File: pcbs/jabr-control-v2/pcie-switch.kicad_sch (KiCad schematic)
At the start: 41 parts, among them U301 SYA75603A, U302 PCI11010C, Y301 XRCGB25M000F3A16R0

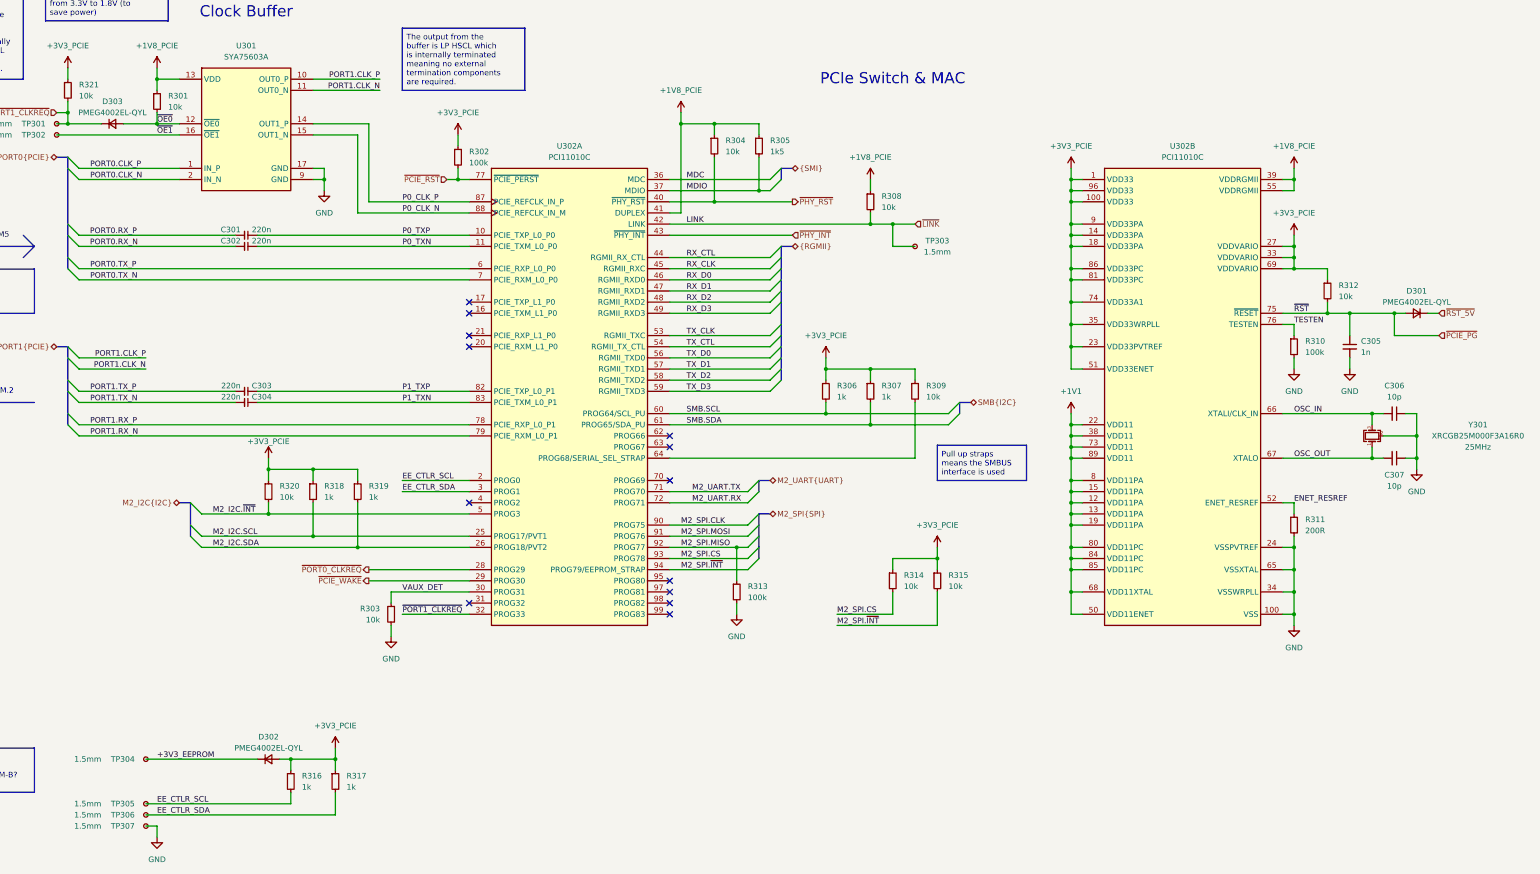
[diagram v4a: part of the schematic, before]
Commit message: Removed power button reset to switch (power will be cycled anyway)
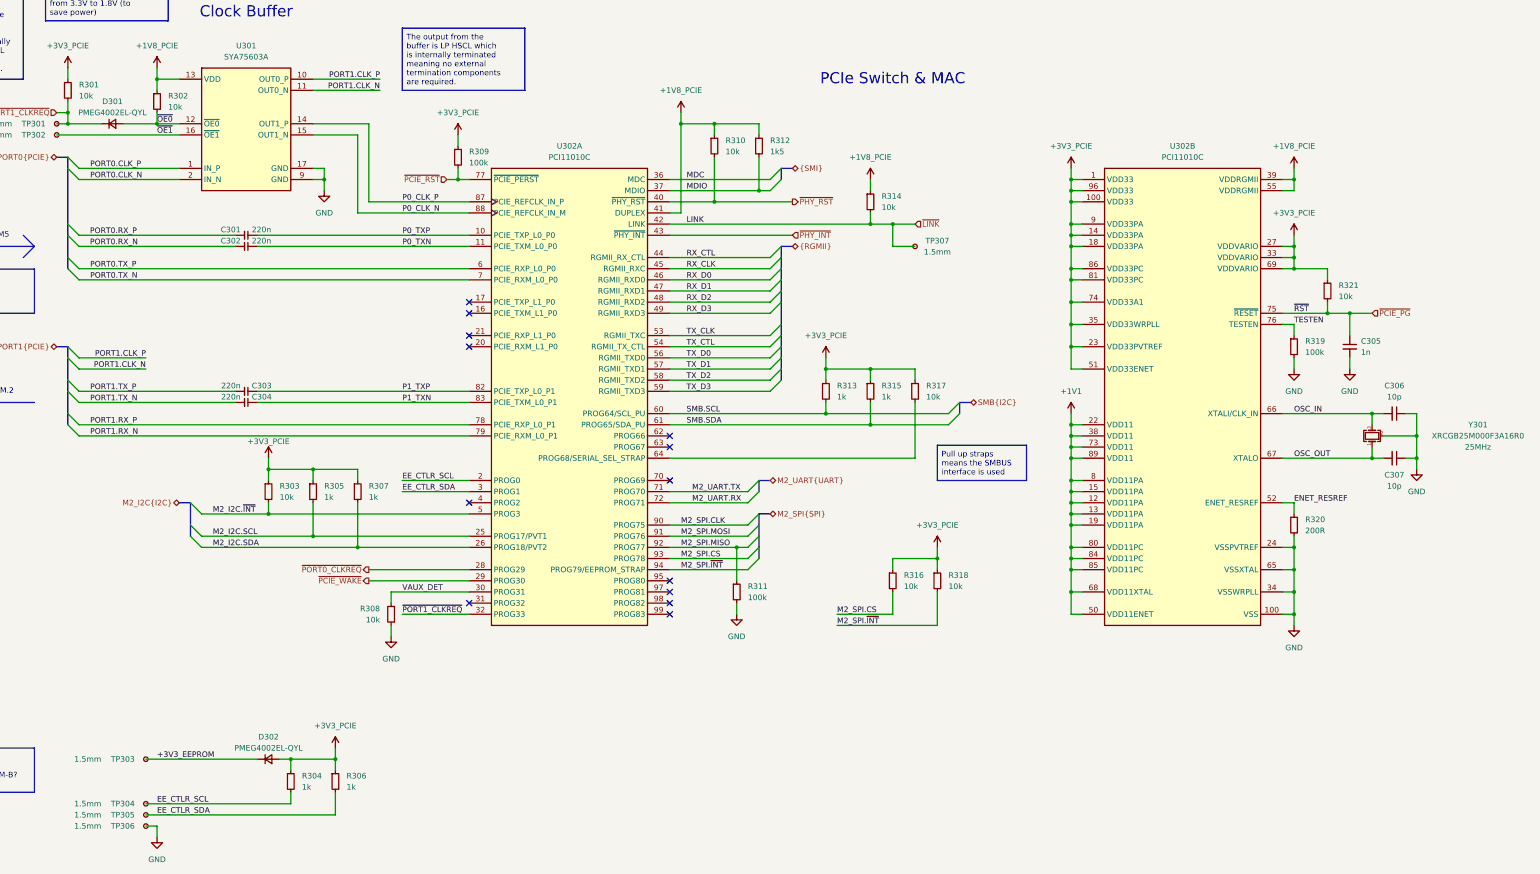
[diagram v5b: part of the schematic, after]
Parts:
- removed D301: PMEG4002EL-QYL, project_footprints:PMEG4002EL-QYL, symbol DIODE:PMEG4002EL-QYL
- renumbered D303 to D301, R321 to R301, R301 to R302, R320 to R303, R316 to R304, R318 to R305, R317 to R306, R319 to R307, R303 to R308, R302 to R309, R304 to R310, R313 to R311, R305 to R312, R306 to R313, R308 to R314, R307 to R315, R314 to R316, R309 to R317, R315 to R318, R310 to R319, R311 to R320, R312 to R321, TP304 to TP303, TP305 to TP304, TP306 to TP305, TP307 to TP306, TP303 to TP307

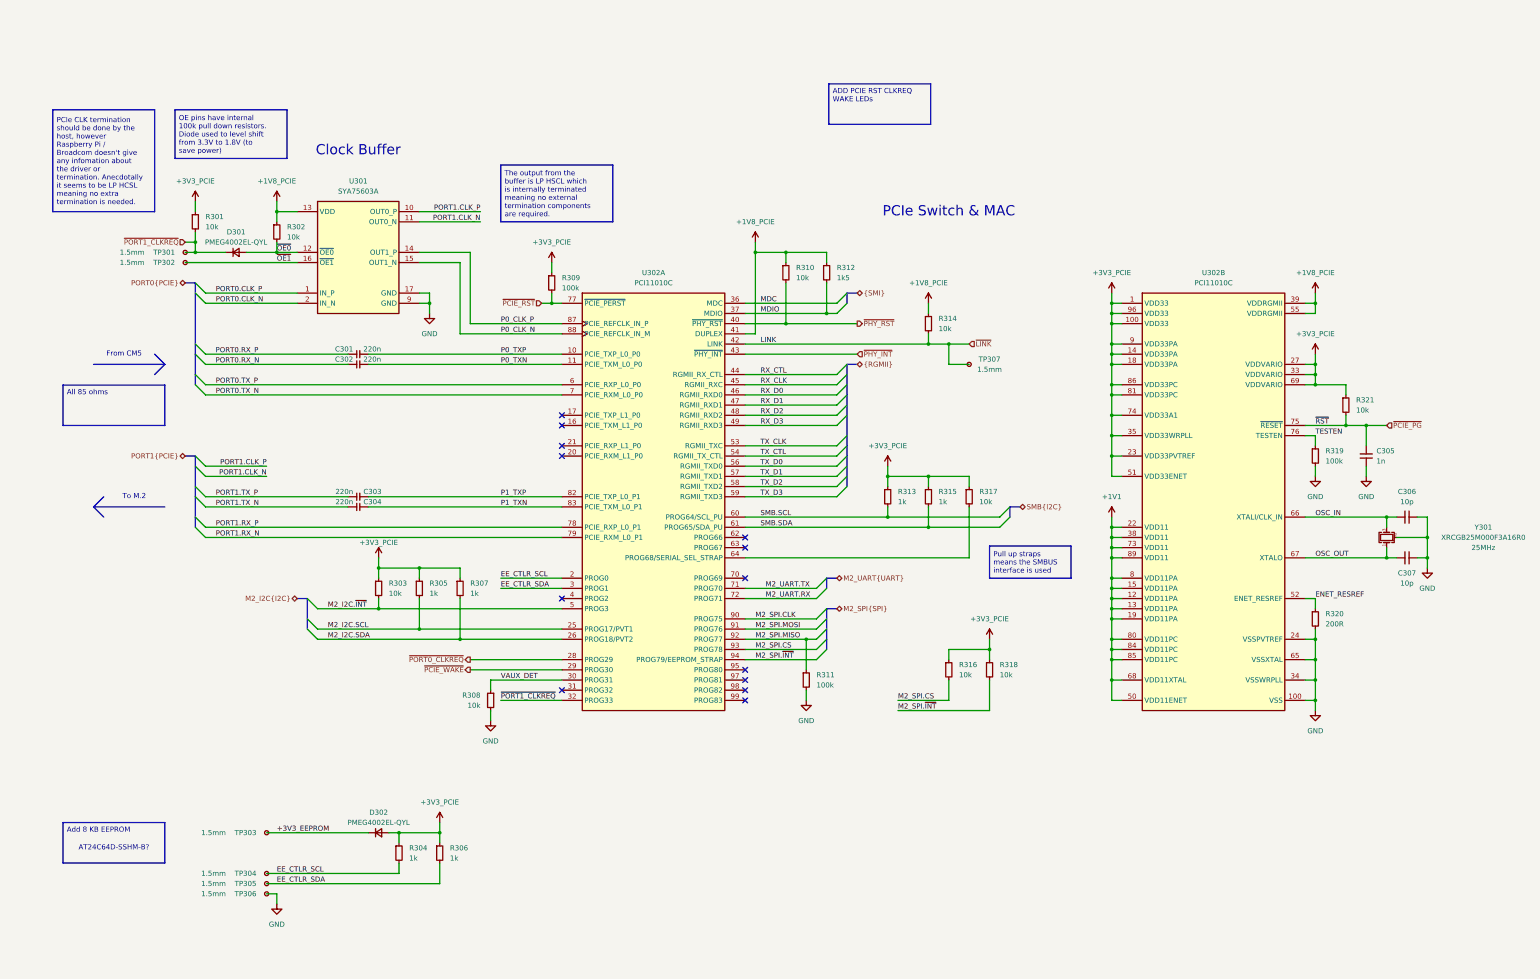
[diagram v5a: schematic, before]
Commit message: Schematic done
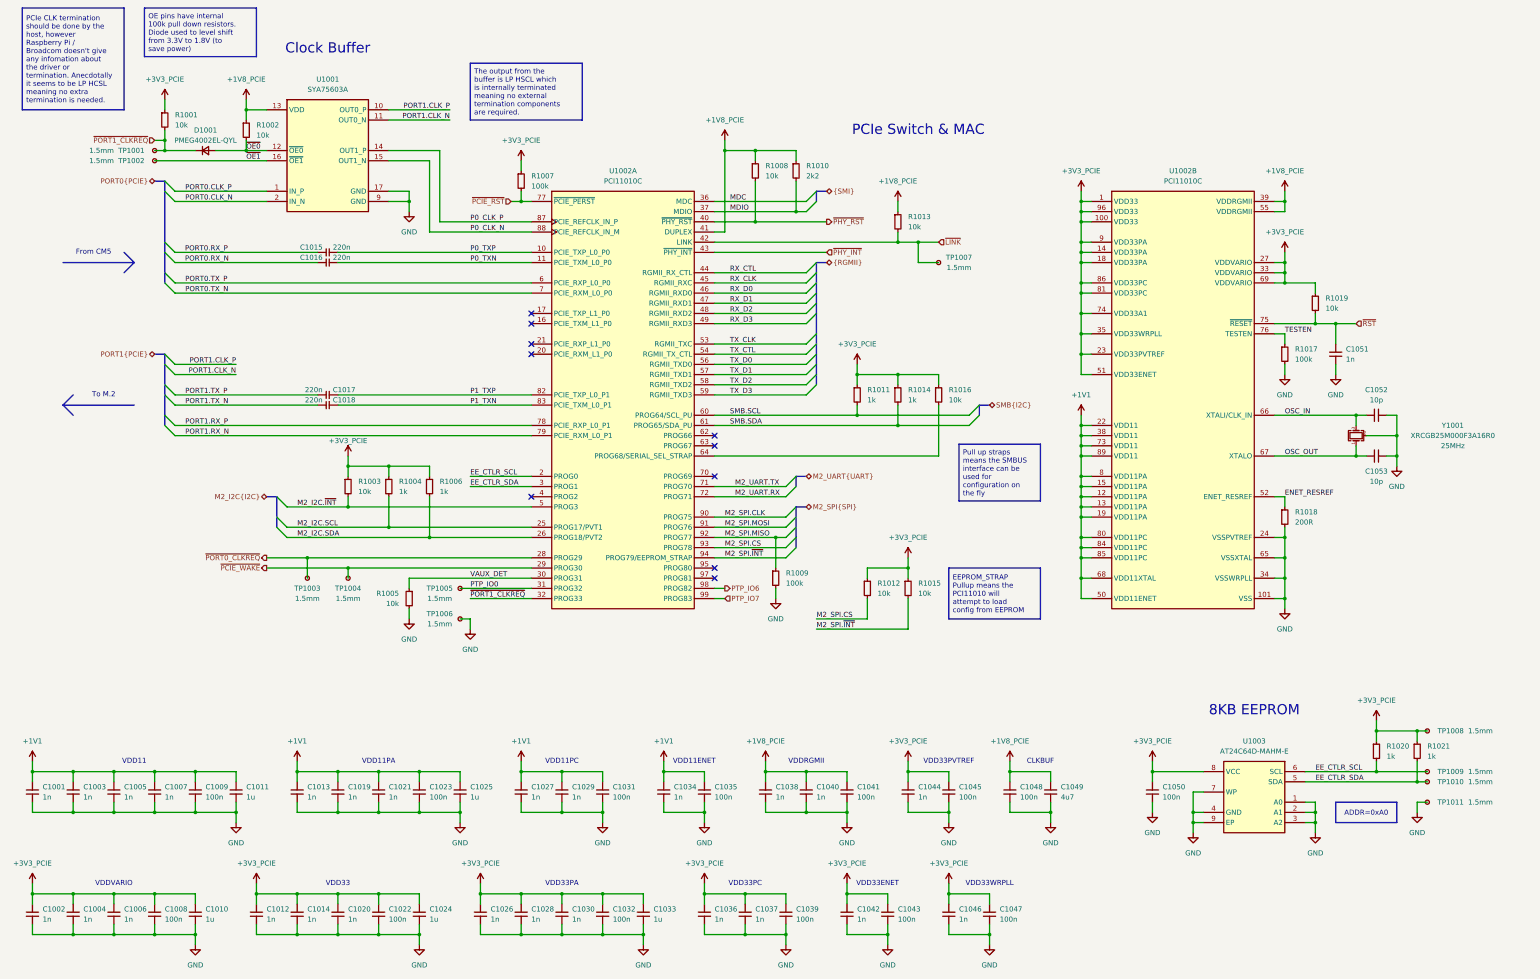
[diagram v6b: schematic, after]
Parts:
- removed D302: PMEG4002EL-QYL, project_footprints:PMEG4002EL-QYL, symbol DIODE:PMEG4002EL-QYL
- removed TP303, TP304, TP305, TP306: 1.5mm, project_footprints:TestPoint_Pad_D1.5mm, symbol Connector:TestPoint_Small
- added C1001, C1002, C1003, C1004, C1005, C1006, C1007, C1012, C1013, C1014, C1019, C1020, C1021, C1026, C1027, C1028, C1029, C1030, C1034, C1036, C1037, C1038, C1040, C1042, C1044, C1046: 1n, project_footprints:C_0402, symbol DEV:C_SMALL
- added C1008, C1009, C1022, C1023, C1031, C1032, C1035, C1039, C1041, C1043, C1045, C1047, C1048, C1050: 100n, project_footprints:C_0402, symbol DEV:C_SMALL
- added C1010, C1011, C1024, C1025, C1033: 1u, project_footprints:C_0402, symbol DEV:C_SMALL
- added C1049: 4u7, project_footprints:C_0402, symbol DEV:C_SMALL
- added TP1003, TP1004, TP1005, TP1006, TP1008, TP1009, TP1010, TP1011: 1.5mm, project_footprints:TestPoint_Pad_D1.5mm, symbol Connector:TestPoint_Small
- added U1003: AT24C64D-MAHM-E, project_footprints:SON50P300X200X60-9N, symbol EEPROM:AT24C64D-MAHM-E
- R1010: renamed from R312; value 1k5 -> 2k2
- renumbered C301 to C1015, C302 to C1016, C303 to C1017, C304 to C1018, C305 to C1051, C306 to C1052, C307 to C1053, D301 to D1001, R301 to R1001, R302 to R1002, R303 to R1003, R305 to R1004, R308 to R1005, R307 to R1006, R309 to R1007, R310 to R1008, R311 to R1009, R313 to R1011, R316 to R1012, R314 to R1013, R315 to R1014, R318 to R1015, R317 to R1016, R319 to R1017, R320 to R1018, R321 to R1019, R304 to R1020, R306 to R1021, TP301 to TP1001, TP302 to TP1002, TP307 to TP1007, U301 to U1001, U302 to U1002, Y301 to Y1001
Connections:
- net +1V1: now also C1001.1, C1003.1, C1005.1, C1007.1, C1009.1, C1011.1, C1013.1, C1019.1, C1021.1, C1023.1, C1025.1, C1027.1, C1029.1, C1031.1, C1034.1, C1035.1
- net +1V8_PCIE: now also C1038.1, C1040.1, C1041.1, C1048.1, C1049.1
- net +3V3_PCIE: now also C1002.1, C1004.1, C1006.1, C1008.1, C1010.1, C1012.1, C1014.1, C1020.1, C1022.1, C1024.1, C1026.1, C1028.1, C1030.1, C1032.1, C1033.1, C1036.1, C1037.1, C1039.1, C1042.1, C1043.1, C1044.1, C1045.1, C1046.1, C1047.1, C1050.1, TP1008.1, U1003.8 (VCC)
- net EE_CTLR_SCL: now also TP1009.1, U1003.6 (SCL)
- net EE_CTLR_SDA: now also TP1010.1, U1003.5 (SDA)
- net GND: now also U1002.101 (VSS), C1001.2, C1002.2, C1003.2, C1004.2, C1005.2, C1006.2, C1007.2, C1008.2, C1009.2, C1010.2, C1011.2, C1012.2, C1013.2, C1014.2, C1019.2, C1020.2, C1021.2, C1022.2, C1023.2, C1024.2, C1025.2, C1026.2, C1027.2, C1028.2, C1029.2, C1030.2, C1031.2, C1032.2, C1033.2, C1034.2, C1035.2, C1036.2, C1037.2, C1038.2, C1039.2, C1040.2, C1041.2, C1042.2, C1043.2, C1044.2, C1045.2, C1046.2, C1047.2, C1048.2, C1049.2, C1050.2, TP1006.1, TP1011.1, U1003.1 (A0), U1003.2 (A1), U1003.3 (A2), U1003.4 (GND), U1003.7 (WP), U1003.9 (EP); no longer U1002.100 (VSS)
- net ~{PCIE_WAKE}: now also TP1004.1
- net ~{PORT0_CLKREQ}: now also TP1003.1
- net PTP_IO0: now reaches U1002.31 (PROG32)
- net PTP_IO0: now also TP1005.1
- net PTP_IO6: now reaches U1002.98 (PROG82)
- net PTP_IO7: now reaches U1002.99 (PROG83)
- net ~{PCIE_PG} renamed ~{RST}
- no-connect marks 13 -> 10
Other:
- note added: "8KB EEPROM"
- note added: "CLKBUF"
- note added: "VDD11"
- note added: "VDD11ENET"
- note added: "VDD11PA"
- note added: "VDD11PC"
- note added: "VDD33"
- note added: "VDD33ENET"
- note added: "VDD33PA"
- note added: "VDD33PC"
- note added: "VDD33PVTREF"
- note added: "VDD33WRPLL"
- note added: "VDDRGMII"
- note added: "VDDVARIO"
- note removed: "AT24C64D-SSHM-B?"
- moved on the sheet: C1015, C1016, C1017, C1018, C1051, C1052, C1053, D1001, R1001, R1002, R1003, R1004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
